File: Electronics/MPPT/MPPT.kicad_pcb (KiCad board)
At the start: 2 copper layers, 172.7 x 116.8 mm, 155 parts, among them J1 Solar Array, J2 Battery, J3 Car Power, J4 CAN_In, J5 CAN_Out, Q1 NMOS, Q2 NMOS, SW1 RESET, SW2 CAN Address, U1 PQMC3-D12-S9-S, U2 Nucleo_L432KC, U3 UCC37321, U4 INA210, U5 ADM3055E, U6 INA210, U7 CDSOT23-T24CAN

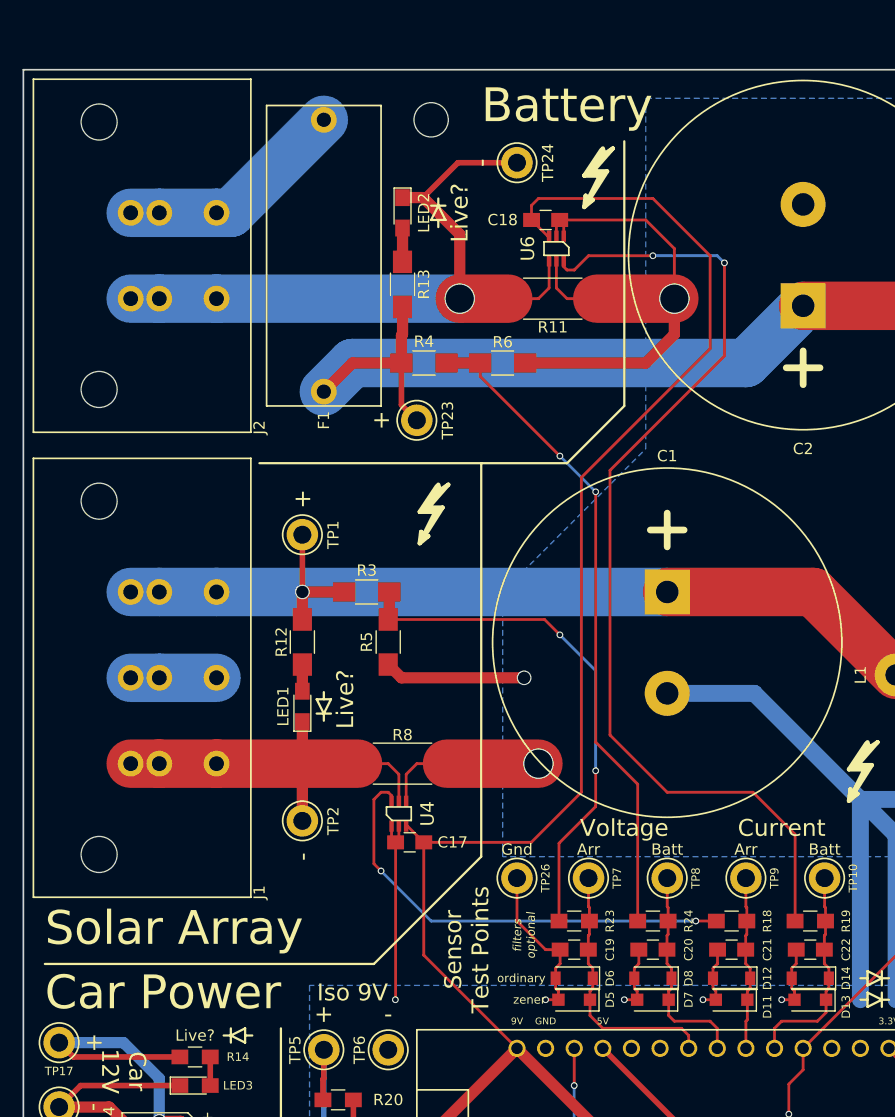
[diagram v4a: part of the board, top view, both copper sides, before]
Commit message: MPPT: Compact sensor blocks on PCB.
By flipping the current sensor onto the back side of the board (makes sense, since that's where the ground plane is), I was able to compact the sensor layout significantly. This will save board space and even make access to the current sensors much easier.
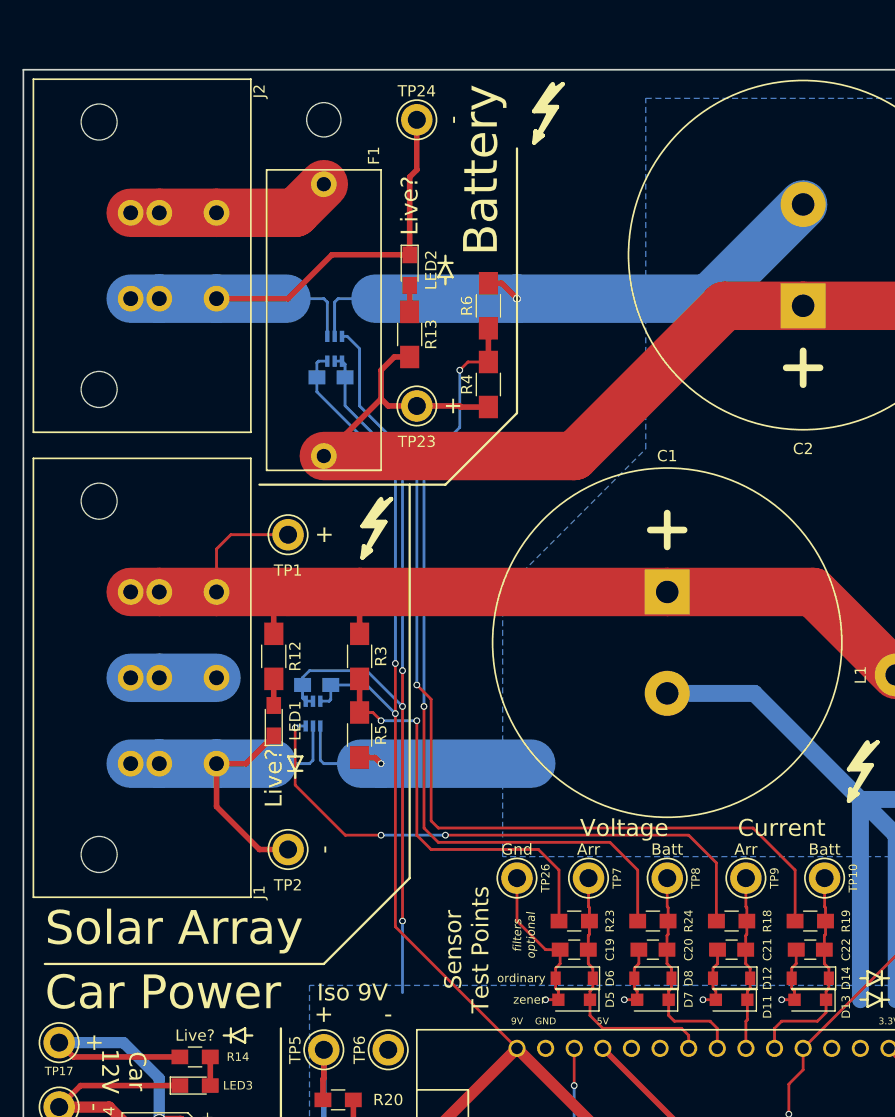
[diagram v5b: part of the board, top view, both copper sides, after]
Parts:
- C17, C18, R11, R8, U4, U6: moved to B.Cu
- moved C18 23.6 mm to (58.4, 58.4)
- moved U6 21.6 mm to (58.7, 55.9)
- moved R11 19.7 mm to (58.4, 51.4)
- moved C17 16.2 mm to (57.1, 85.7)
- moved U4 11.7 mm to (56.8, 88.3)
- moved TP24 9.67 mm to (66.0, 35.6)
- moved REF** 9.53 mm to (57.8, 35.6)
- moved R5 8.64 mm to (61.0, 90.2)
- moved R8 7.62 mm to (57.1, 92.7)
- moved REF** 7.24 mm to (76.8, 35.6)
- moved R4 6.02 mm to (72.4, 59.1), turned to 90 degrees
- moved R3 5.75 mm to (61.0, 83.2), turned to 270 degrees
- moved F1 5.72 mm to (57.8, 53.3)
- moved REF** 5.68 mm to (55.2, 92.7)
- moved R6 5.24 mm to (72.4, 52.1), turned to 90 degrees
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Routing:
- net GNDPWR: track 409.7 -> 463.5 mm, vias 22 -> 23
- net +9VA: track 319.1 -> 283.6 mm, vias 4 -> 6
- net Net-(R24-Pad1): track 58.3 -> 72.8 mm
- net Net-(R18-Pad1): track 40.7 -> 51.5 mm, vias 2 -> 3
- net /-Batt: track 61.7 -> 51.6 mm, vias 1 -> 0
- net Net-(R23-Pad1): track 46.2 -> 37.0 mm
- net /+Arr: track 82.2 -> 89.1 mm, vias 1 -> 0
- net /+Batt: track 109.8 -> 116.1 mm
- net Net-(R19-Pad1): track 89.6 -> 85.2 mm, vias 2 -> 1
- net Net-(F1-Pad1): track 20.6 -> 18.2 mm
- net /-Arr: track 35.4 -> 37.2 mm
- net Net-(LED2-Pad2): track 3.00 -> 2.37 mm
